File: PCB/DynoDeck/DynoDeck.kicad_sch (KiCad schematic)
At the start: 60 parts, among them J1 USB_C_Receptacle_USB2.0_16P, J2 E-paper, J3 CardKB, J4 PGRM, SW1 QON, SW2 RESET, SW4 SW_DPDT_x2, U1 E73-2G4M08S1C, U2 SX1262IMLTRT, U3 BQ25895RTW, U4 AMS1117-3.3, U5 BGS12WN6E6327, U6 USBLC6-2SC6, Y1 32.768kHz, Y2 OW7EL89CENUXK7YLC-32M

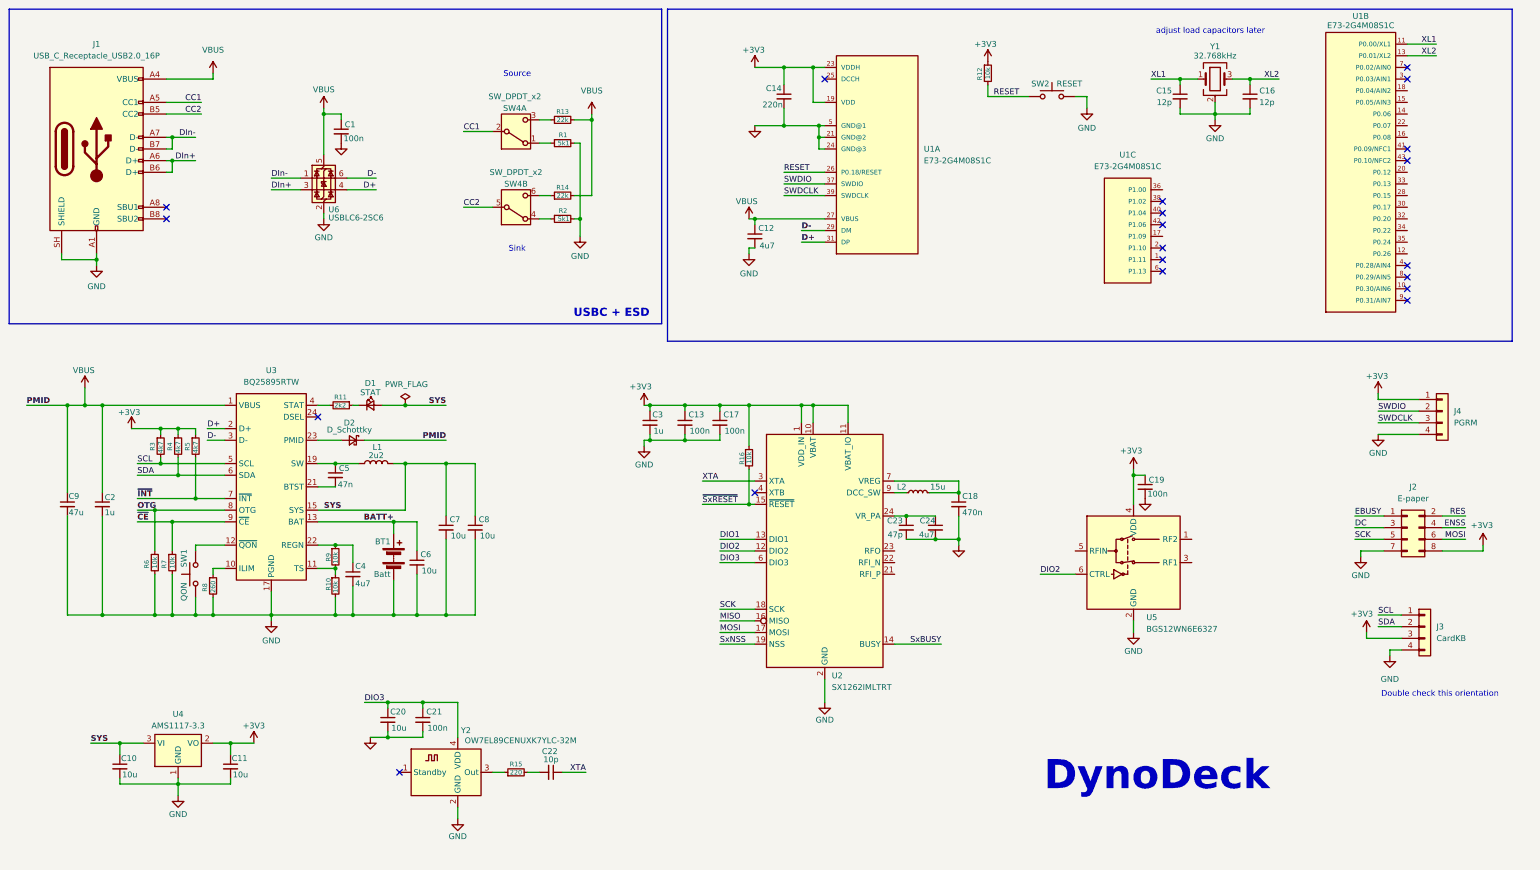
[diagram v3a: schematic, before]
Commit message: Sx1262 RF Signals mostly wired
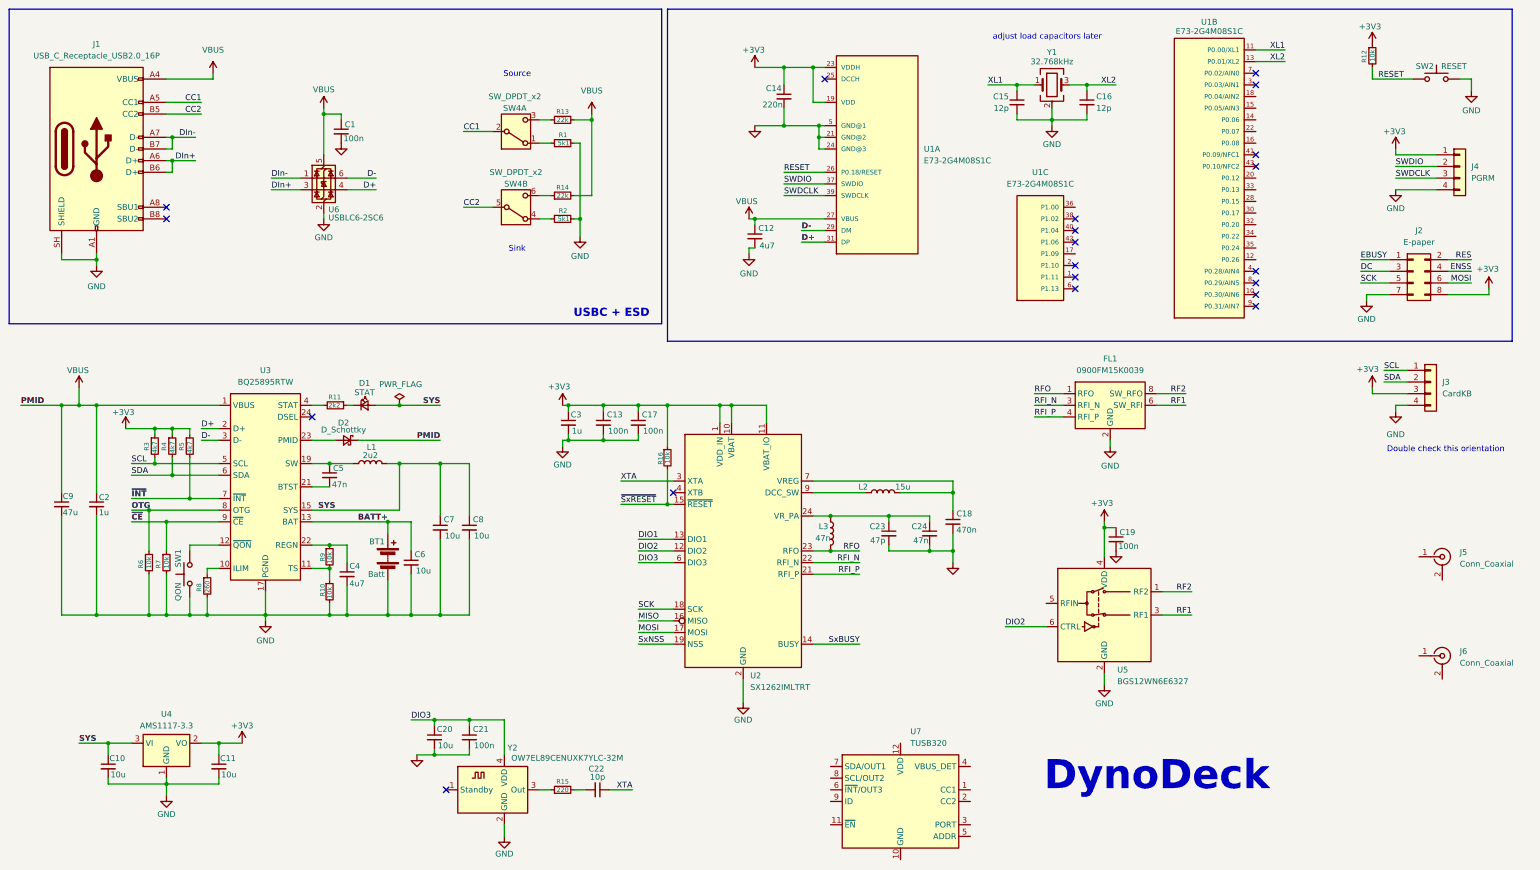
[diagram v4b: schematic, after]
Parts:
- removed L2: 15u, symbol Device:L_Small
- added FL1: 0900FM15K0039, RF_Converter:Balun_Johanson_0900FM15K0039, symbol Filter:0900FM15K0039
- added J5, J6: Conn_Coaxial, symbol Connector:Conn_Coaxial
- added L2: 15u, symbol Device:L
- added L3: 47n, symbol Device:L
- added U7: TUSB320, Package_DFN_QFN:Texas_X2QFN-12_1.6x1.6mm_P0.4mm, symbol Interface_USB:TUSB320
- C24: value 4u7 -> 47n
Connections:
- net GND: now also FL1.10 (GND), FL1.2 (GND), FL1.5 (GND), FL1.7 (GND), FL1.9 (GND)
- net at C18.1, U2.7 (VREG): now also L2.2
- net at U2.9 (DCC_SW): now also L2.1
- net RF2: now reaches U5.1 (RF2)
- net RF2: now also FL1.8 (SW_RFO)
- net RF1: now reaches U5.3 (RF1)
- net RF1: now also FL1.6 (SW_RFI)
- net at C23.1, C24.1, U2.24 (VR_PA): now also L3.2
- net RFI_P: now reaches U2.21 (RFI_P)
- net RFI_P: now also FL1.4 (RFI_P)
- net RFI_N: now reaches U2.22 (RFI_N)
- net RFI_N: now also FL1.3 (RFI_N)
- net RFO: now reaches U2.23 (RFO)
- net RFO: now also FL1.1 (RFO), L3.1
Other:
- moved on the sheet: BT1, C10, C11, C13, C15, C16, C17, C18, C19, C2, C20, C21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

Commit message: RF wiring
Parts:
- added C25: 100n, symbol Device:C_Small
- added C26: 100p, symbol Device:C_Small
- added R17: 47, symbol Device:R_Small
- added U8: BGS12WN6E6327, Package_LGA:Infineon_PG-TSNP-6-10_0.7x1.1mm_0.7x1.1mm_P0.4mm, symbol RF_Switch:BGS12WN6E6327
- R11: value 2k2 -> 5k1
- U4: value AMS1117-3.3 -> SSP7903P33FR
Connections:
- net +3V3: now also C25.1, U8.4 (VDD)
- net DIO2: now also R17.1; no longer U5.6 (CTRL)
- net GND: now also J5.2 (Ext), J6.2 (Ext), C25.2, U8.2 (GND)
- net SCL: now also U1.17 (P1.09)
- net SDA: now also U1.36 (P1.00)
- net ANT2: now reaches J6.1 (In)
- net ANT2: now also U8.1 (RF2)
- net RFIN_A: now reaches U5.5 (RFIN)
- net RFIN_A: now also C26.1
- net ANT1: now reaches J5.1 (In)
- net ANT1: now also U8.3 (RF1)
- net RF1 renamed SW_RFI
- net RF2 renamed SW_RFO
- new net: C26.2, U8.5 (RFIN)
- new net: R17.2, U5.6 (CTRL)
- new net ANT_CTRL: U8.6 (CTRL)
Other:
- moved on the sheet: BT1, C10, C11, C13, C15, C16, C17, C18, C19, C2, C20, C21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

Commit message: TUSB320 Wiring
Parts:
- removed C20: 10u, symbol Device:C_Small
- added C27: 100n, symbol Device:C_Small
- added FB1: 600@100Mhz, symbol Device:FerriteBead_Small
- added R18: 887k, symbol Device:R
- added R19, R20, R21: 100k, symbol Device:R_Small
- R5: value 4k7 -> 10k
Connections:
- net +3V3: now also U7.12 (VDD), C27.1, R19.1, R20.1, R21.1
- net CC1: now also U7.1 (CC1)
- net CC2: now also U7.2 (CC2)
- net DIO3: now also FB1.1; no longer C21.1, Y2.4 (VDD)
- net GND: now also U7.10 (GND), U7.11 (~{EN}), C27.2
- net VBUS: now also R18.2
- net at U7.4 (VBUS_DET): now also R18.1
- net OUT1: now reaches U7.7 (SDA/OUT1)
- net OUT1: now also R21.2
- net OUT2: now reaches U7.8 (SCL/OUT2)
- net OUT2: now also R20.2
- net ID: now reaches U7.9 (ID)
- net ID: now also R19.2
- new net: C21.1, FB1.2, Y2.4 (VDD)
- no-connect marks 20 -> 23
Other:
- moved on the sheet: C12, C14, C15, C16, C21, J2, J3, J4, J5, J6, R12, SW2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

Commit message: organize
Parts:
- removed D2: D_Schottky, symbol Device:D_Schottky_Small
- removed R1, R2: 5k1, symbol Device:R_Small
- removed R13, R14: 22k, symbol Device:R_Small
- removed SW4: SW_DPDT_x2, symbol Switch:SW_DPDT_x2
- added D3: D_Schottky, symbol Device:D_Schottky
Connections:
- net VBUS: now also D3.1 (K)
- net at U3.23 (PMID): now also D3.2 (A)
- net RFIN_A renamed SW_ANT
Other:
- note added: "Battery Charger"
- note added: "RF Filter + Switch"
- note added: "Sx1262"
- note added: "nRF52840"
- note removed: "Sink"
- note removed: "Source"
- moved on the sheet: BT1, C1, C10, C11, C13, C17, C18, C19, C2, C21, C22, C23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

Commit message: Reorganize + new LDO
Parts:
- removed U4: SSP7903P33FR, Package_TO_SOT_SMD:SOT-223-3_TabPin2, symbol Regulator_Linear:AMS1117-3.3
- added SW3: SW_SPDT, symbol Switch:SW_SPDT
- added U9: MD7218E33PC1, Package_TO_SOT_SMD:SOT-89-5, symbol Regulator_Linear:AP2112K-3.3
- C10, C11: value 10u -> 4u7
- J5: value Conn_Coaxial -> u.FL
- J6: value Conn_Coaxial -> SMA
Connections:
- net +3V3: now also U9.5 (VOUT)
- net ANT_CTRL: now also U1.7 (P0.02/AIN0)
- net DC: now also U1.16 (P0.08)
- net DIO1: now also U1.18 (P0.04/AIN2)
- net EBUSY: now also U1.35 (P0.24)
- net ENSS: now also U1.34 (P0.22)
- net GND: now also SW3.3 (C), U9.2 (GND)
- net ID: now also U1.3 (P0.03/AIN1)
- net MISO: now also U1.33 (P0.13)
- net MOSI: now also U1.32 (P0.20)
- net OTG: now also U1.10 (P0.30/AIN6)
- net OUT1: now also U1.1 (P1.11)
- net OUT2: now also U1.2 (P1.10)
- net RES: now also U1.28 (P0.15)
- net SCK: now also U1.30 (P0.17)
- net SCL: now also U1.14 (P0.06); no longer U1.17 (P1.09)
- net SDA: now also U1.15 (P0.05/AIN3); no longer U1.36 (P1.00)
- net SYS: now also SW3.1 (A), U9.4 (NC)
- net SxBUSY: now also U1.17 (P1.09)
- net SxNSS: now also U1.22 (P0.07)
- net ~{CE}: now also U1.9 (P0.31/AIN7)
- net ~{INT}: now also U1.8 (P0.29/AIN5)
- net ~{SxRESET}: now also U1.36 (P1.00)
- new net EN: SW3.2 (B), U9.3 (EN)
- no-connect marks 23 -> 18
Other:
- note added: "pref not use cuz crystal"
- note removed: "Battery Charger"
- note removed: "RF Filter + Switch"
- note removed: "Sx1262"
- note removed: "USBC + ESD"
- note removed: "nRF52840"
- moved on the sheet: BT1, C1, C10, C11, C12, C13, C14, C15, C16, C17, C18, C19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
